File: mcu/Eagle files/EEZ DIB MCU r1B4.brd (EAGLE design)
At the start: 139 x 70 mm, 195 parts, among them IC1 TPD4E001DRLR, IC10 TPS61169DCKR, IC11 TPD4E001DRLR, IC12 TPA6205A1DGN, IC13 TPD4E001DRLR, IC14 TSC2007IPW, IC15 TPD4E001DRLR, IC16 DP83848CVV/NOPB, IC2 SN74LVC2G34DBVR, IC3 BTS3408G, IC4 STM32F769IGT6, IC5 LD1117ADT33TR, IC6 TPD4E001DRLR, IC7 IS42S16400J, IC8 AT24C256C-SSHL-B, IC9 TPS2051BDBVR, J1 503398-1892, J2 67803-8020, Q1 MMBT5551, SW1 TL1100CF160Q, SW2 PEC16-2215F-S0024, SW3 JS102011SAQN, X1 ZL263-40DG, X2 ZL231-16KG, X3 1844249, X4 22-23-2061, X5 LMJTAB881243M-L, Y1 25MHz, Y2 XTAL016178-85SMX

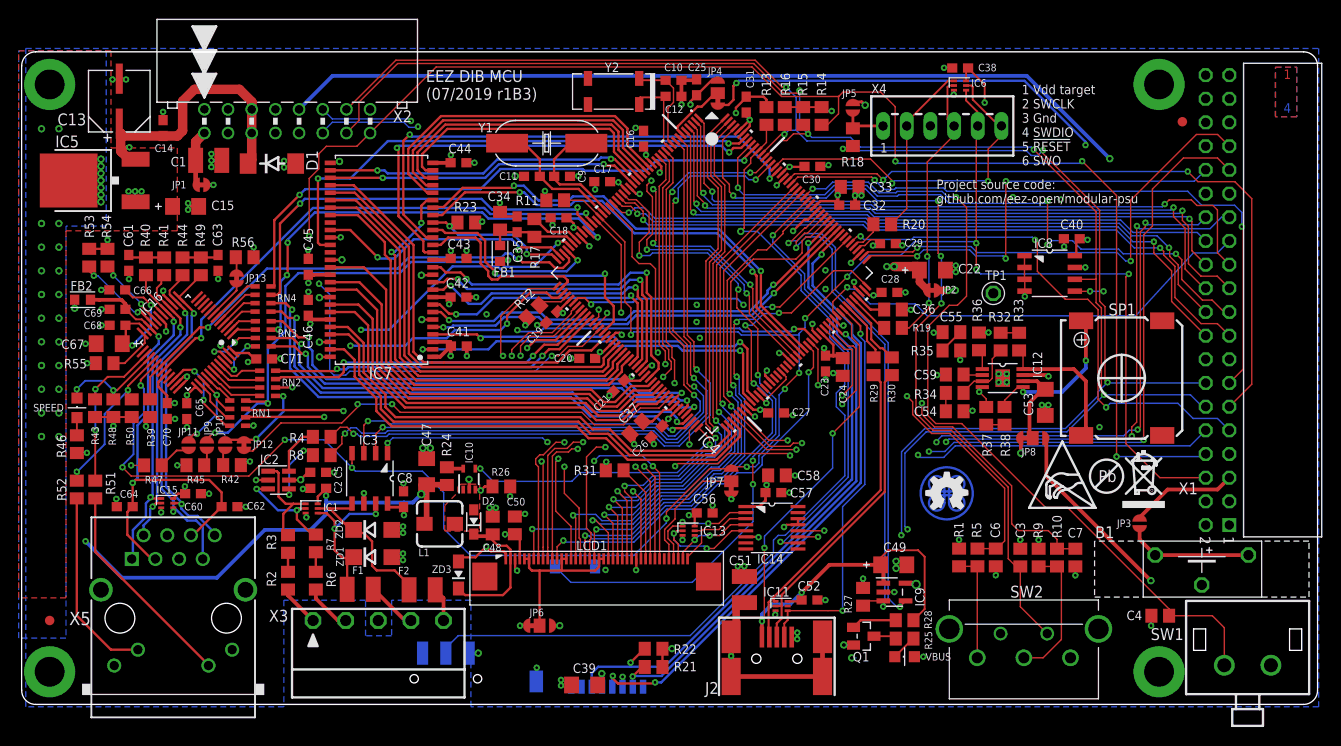
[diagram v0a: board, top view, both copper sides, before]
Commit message: MCU board chages for #37, #42
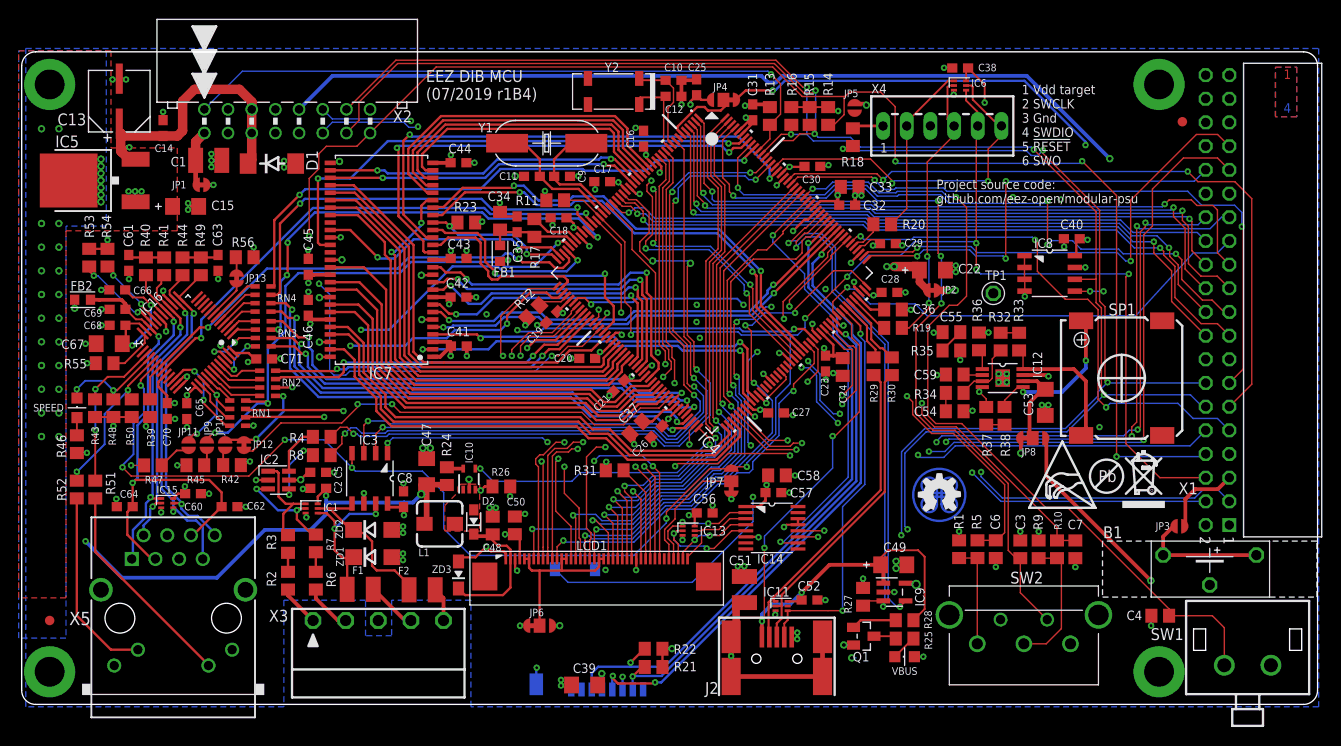
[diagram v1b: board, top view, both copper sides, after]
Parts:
- removed SW3: JS102011SAQN, EEZ_switches:JS102011SAQN
- moved JP3 4.28 mm to (119.7, 19.1), turned to 0 degrees
- moved SW2 1.50 mm to (103.0, 6.50)
- moved C31 1.08 mm to (73.9, 63.5)
- moved JP4 0.95 mm to (70.8, 64.8), turned to 180 degrees
- moved C3 0.89 mm to (102.6, 16.6)
- moved C7 0.89 mm to (108.5, 16.6)
- moved R10 0.89 mm to (106.6, 16.6)
- moved R9 0.89 mm to (104.6, 16.6)
- moved C6 0.89 mm to (100.0, 16.6)
- moved R1 0.89 mm to (96.1, 16.6)
- moved R5 0.89 mm to (98.0, 16.6)
- moved B1 0.85 mm to (122.9, 16.0)
- moved EEZ_SIGNATURE 0.82 mm to (93.9, 22.5)
- moved R14 0.70 mm to (82.0, 63.1)
- moved R15 0.70 mm to (80.0, 63.1)
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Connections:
- removed net DIN1: IC4.7, R4.2
- removed net DOUT1: IC3.2, IC4.162
- new net UART_RX/DIN1: IC4.24, R4.2, X1.3
- new net UART_TX/DOUT1: IC3.2, IC4.162, X1.4
- net +3V3: no longer SW3.1
- net BOOT0: now also X2.2; no longer SW3.2
- net PE: no longer X2.2
- net SD_DETECT: now also IC4.140; no longer IC4.24
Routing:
- net UART_RX/DIN1: track 0.00 -> 142.7 mm, vias 0 -> 7
- net UART_TX/DOUT1: track 0.00 -> 141.0 mm, vias 0 -> 7
- net DOUT1: track 76.5 -> 0.00 mm, vias 4 -> 0
- net DIN1: track 74.7 -> 0.00 mm, vias 2 -> 0
- net BOOT0: track 97.0 -> 72.3 mm
- net SD_DETECT: track 73.8 -> 59.7 mm, vias 5 -> 4
- net N$20: track 117.6 -> 114.3 mm
- net PE: track 184.9 -> 182.3 mm
- net ENC_B: track 46.2 -> 43.6 mm
- net GND: track 153.6 -> 151.4 mm, vias 155 -> 154
- net +VAUX: track 149.8 -> 147.8 mm
- net I2C1_SDA: track 177.4 -> 179.2 mm
- net N$51: track 4.91 -> 3.34 mm
- net I2C1_SCL: track 178.3 -> 179.7 mm
- net ENC_SW: track 86.3 -> 85.0 mm
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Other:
- board text added: "EEZ DIB MCU (07/2019 r1B4)"
- board text removed: "EEZ DIB MCU (07/2019 r1B3)"

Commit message: MCU board Vdd trace fixed
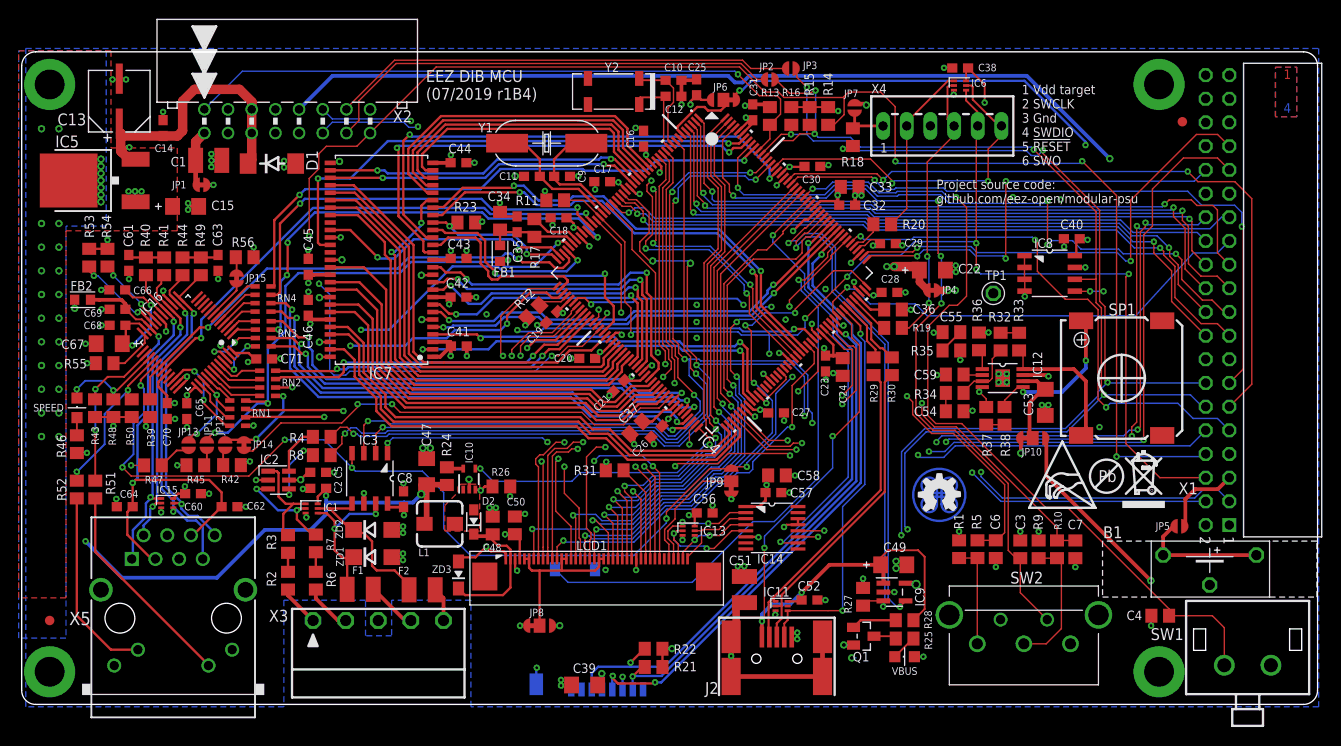
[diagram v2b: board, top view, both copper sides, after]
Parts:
- added JP14, JP15: JP2-NOCUT, EEZ_Lib1:JP2-NOCUT
- JP10, JP9: value JP2-CUT -> JP3-CUT; device EEZ_Lib1:JP2-CUT -> EEZ_Lib1:JP3-CUT
- JP12, JP13, JP2: value JP2-NOCUT -> JP2-CUT; device EEZ_Lib1:JP2-NOCUT -> EEZ_Lib1:JP2-CUT
- JP4: value JP3-CUT -> JP2-NOCUT; device EEZ_Lib1:JP3-CUT -> EEZ_Lib1:JP2-NOCUT
- JP7: value JP3-CUT -> JP2-CUT; device EEZ_Lib1:JP3-CUT -> EEZ_Lib1:JP2-CUT
- moved JP10 86.6 mm to (103.9, 28.6), turned to 0 degrees
- moved JP3 64.4 mm to (78.0, 68.2)
- moved JP6 59.7 mm to (70.8, 64.8), turned to 180 degrees
- moved JP5 56.8 mm to (119.7, 19.1), turned to 0 degrees
- moved JP8 56.6 mm to (51.1, 8.45)
- moved JP9 56.4 mm to (71.6, 23.9), turned to 90 degrees
- moved JP7 42.2 mm to (84.8, 64.0), turned to 270 degrees
- moved JP4 30.3 mm to (93.2, 44.4), turned to 0 degrees
- moved JP2 28.6 mm to (75.7, 67.0), turned to 180 degrees
- moved JP13 18.6 mm to (13.4, 27.8), turned to 90 degrees
- moved JP12 2.02 mm to (17.3, 27.8)
- moved JP11 1.96 mm to (15.4, 27.8), turned to 270 degrees
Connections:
- new net N$13: JP3.1, X2.14
- new net N$7: JP2.2, X2.13
- net !RESET: now also JP9.NO; no longer JP7.NO
- net +3V3: now also JP10.NC, JP4.2, JP7.1, JP8.NO; no longer JP2.2, JP5.1, JP6.NO, JP8.NC
- net +5V: now also JP10.NO; no longer JP8.NO
- net +VAUX: now also JP5.2; no longer JP3.2
- net ETH_CRS: now also JP11.1; no longer JP9.1
- net ETH_RX_ER: now also JP14.1; no longer JP10.1
- net ETH_RX_ERR: now also JP14.2; no longer JP12.2
- net GND: now also JP8.NC, JP9.NC; no longer JP6.NC, JP7.NC
- net I2C1_SCL: now also JP2.1; no longer X2.13
- net I2C1_SDA: now also JP3.2; no longer X2.14
- net N$11: now also JP13.2; no longer JP11.2
- net N$20: now also JP5.1, JP6.NC; no longer JP3.1, JP4.NC
- net N$23: now also JP13.1; no longer JP11.1
- net N$24: now also JP9.COM; no longer JP7.COM
- net N$25: now also JP11.2; no longer JP9.2
- net N$26: now also JP12.2; no longer JP10.2
- net N$27: now also JP15.2; no longer JP13.2
- net N$28: now also JP15.1; no longer JP13.1
- net N$4: now also JP8.COM; no longer JP6.COM
- net N$51: now also JP7.2; no longer JP5.2
- net N$52: now also JP10.COM; no longer JP8.COM
- net VBAT: now also JP6.COM; no longer JP4.COM
- net VDD: now also JP4.1, JP6.NO; no longer JP2.1, JP4.NO
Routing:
- net I2C1_SCL: track 179.7 -> 128.7 mm
- net I2C1_SDA: track 179.2 -> 128.9 mm
- net N$7: track 0.00 -> 49.8 mm
- net N$13: track 0.00 -> 49.6 mm
- net SD_DETECT: track 59.7 -> 62.6 mm, vias 4 -> 1
- net N$51: track 3.34 -> 5.09 mm
- net UART_TX/DOUT1: track 141.0 -> 142.2 mm, vias 7 -> 6
- net !RESET: track 236.9 -> 238.1 mm, vias 12 -> 14
- net BOOT0: track 72.3 -> 71.3 mm
- net MCLK_25: track 76.2 -> 75.4 mm
- net LTDC_R2: track 60.9 -> 61.6 mm
- net LTDC_CLK: track 36.9 -> 36.3 mm
- net GND: track 151.4 -> 151.2 mm, vias 154 -> 155
- net UART_RX/DIN1: track 142.7 -> 142.9 mm, vias 7 -> 6

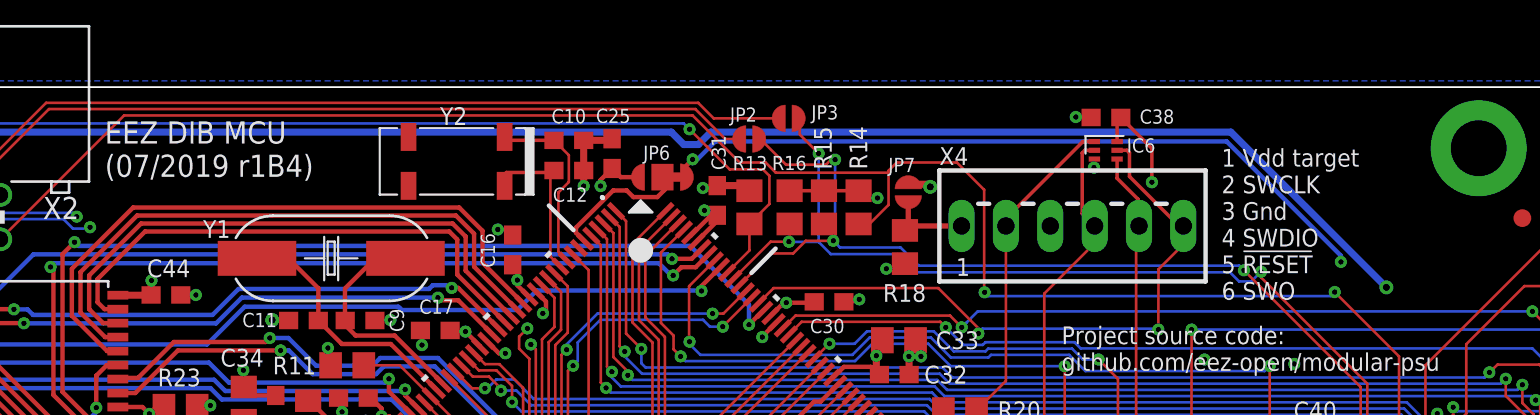
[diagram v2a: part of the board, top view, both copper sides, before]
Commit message: #37, place for optional jumper added
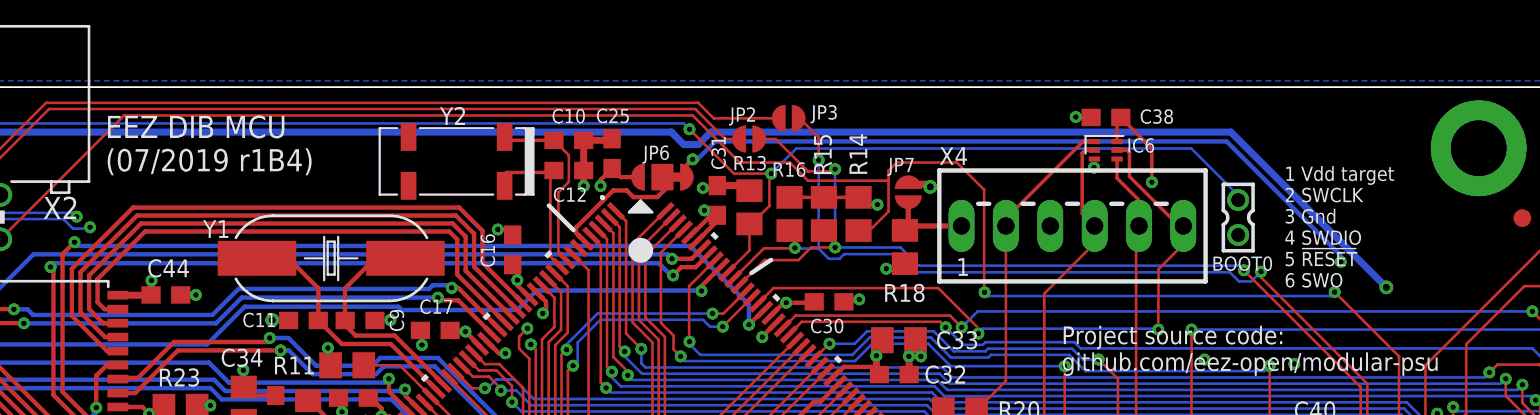
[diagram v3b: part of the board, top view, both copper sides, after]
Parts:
- added BOOT0: (no value), EEZ_Lib1:2MM-2
- moved R14 0.38 mm to (82.0, 62.7)
- moved R15 0.38 mm to (80.0, 62.7)
- moved R16 0.38 mm to (78.1, 62.7)
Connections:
- net +3V3: now also BOOT0.2
- net BOOT0: now also BOOT0.1
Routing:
- net BOOT0: track 71.3 -> 100.3 mm, vias 1 -> 2
- net I2C1_SDA: track 128.9 -> 129.5 mm
- net !FAULT: track 225.0 -> 225.5 mm
